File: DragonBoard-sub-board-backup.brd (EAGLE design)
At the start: 85.1 x 54 mm, 77 parts, among them IC1 REG1117, IC2 93AA76A, Q2 8MHz, U1 TXB0108PWR, U2 TXB0108PWR, U3 62674-301121ALF, U4 62674-301121ALF, U5 NC7ST04M5X

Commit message: Done with baord
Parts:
- removed .1UF, .1UF1, .1UF2, .1UF3, .1UF4, 4.7UF, 4.7UF1, 4.7UF2, 4.7UF3, 4.7UF4, 4.7UF5: (no value), rcl:C0402
- added C100, C102, C104, C106, C107, C108, C109, C110: 0.1uF, rcl:C0402
- added C101, C103, C105: 4.7uF, rcl:C0402
- added C31, C32: 0.1uF, rcl:C0805
- added JP11, JP12, JP13: (no value), pinhead:1X04
- C1, C10, C11, C12, C13, C14, C15, C16, C17, C18, C19, C20, C21, C22, C23, C24, C28, C30, C4, C5, C8, C9: value (none) -> 0.1uF
- C2, C3: value (none) -> 0.1Uf
- C25, C26: value (none) -> 30pF
- C27, C29: value (none) -> 4.7uF
- C6, C7: value (none) -> 1uF
- L1, L2: value (none) -> 0.1uH
- Q2: value 8MHz -> 12MHz
- R1: value (none) -> 1K
- R2, R3: value (none) -> 100k
- R4: value (none) -> 12k
- R5: value (none) -> 22k
- U$1: value DRAGON-BOARD -> DRAGON-BOARD-TH; device DragonBoard:DROGENBOARD -> DragonBoard:DROGENBOARD-TH
- moved JP8 91.2 mm to (93.0, 3.43)
- moved C28 79.1 mm to (65.9, 5.59)
- moved C27 64.2 mm to (77.5, 18.7)
- moved L1 60.8 mm to (60.5, 8.51)
- moved R5 60.7 mm to (73.5, 18.2), turned to 270 degrees
- moved U$4 60.1 mm to (75.6, 10.0)
- moved C29 59.4 mm to (82.3, 15.1), turned to 0 degrees
- moved C30 58.8 mm to (66.7, 10.9)
- moved R4 58.8 mm to (66.7, 9.78)
- moved L2 58.8 mm to (60.3, 11.7)
- moved Q2 57.9 mm to (66.9, 16.3), turned to 180 degrees
- moved C25 57.5 mm to (62.9, 19.3)
- moved R1 57.3 mm to (68.3, 3.05)
- moved R2 57.0 mm to (67.1, 3.05)
- moved IC2 56.8 mm to (73.5, 21.8)
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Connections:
- removed net 3.3V: IC2.6
- removed net SBUS_RX: JP8.2, U5.4
- removed net SBUS_TX: JP8.1
- new net ADBUS_RX: JP8.2, U$4.17, U5.4
- new net ADBUS_TX: JP8.1, U$4.16
- new net BDBUS_RX: JP11.2, U$4.27
- new net BDBUS_TX: JP11.1, U$4.26
- new net CDBUS_RX: JP12.2, U$4.39
- new net CDBUS_TX: JP12.1, U$4.38
- new net DDBUS_RX: JP13.2, U$4.52
- new net DDBUS_TX: JP13.1, U$4.48
- net +3.3V: now also C100.1, C101.1, C108.1, C109.1, C110.1, C31.1, C32.1, IC2.6, JP11.3, JP12.3, JP13.3; no longer .1UF.1, .1UF4.1, 4.7UF.1, 4.7UF4.1, 4.7UF5.1
- net GND: now also C100.2, C101.2, C102.2, C103.2, C104.2, C105.2, C106.2, C107.2, C108.2, C109.2, C110.2, C31.2, C32.2, JP11.4, JP12.4, JP13.4; no longer .1UF.2, .1UF1.2, .1UF2.2, .1UF3.2, .1UF4.2, 4.7UF.2, 4.7UF1.2, 4.7UF2.2, 4.7UF3.2, 4.7UF4.2, 4.7UF5.2
- net VCORE: now also C106.1, C107.1; no longer .1UF3.1, 4.7UF3.1
- net VPHY: now also C104.1, C105.1; no longer .1UF2.1, 4.7UF2.1
- net VPLL: now also C102.1, C103.1; no longer .1UF1.1, 4.7UF1.1
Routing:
- net +3.3V: track 264.2 -> 378.5 mm, vias 9 -> 13
- net +5V: track 126.3 -> 171.6 mm, vias 10 -> 12
- net VCORE: track 0.00 -> 41.1 mm
- net GND: track 30.9 -> 65.2 mm, vias 21 -> 51
- net USB_D+: track 17.9 -> 42.8 mm, vias 0 -> 1
- net ADBUS_RX: track 0.00 -> 23.9 mm, vias 0 -> 1
- net DDBUS_RX: track 0.00 -> 21.8 mm, vias 0 -> 2
- net ADBUS_TX: track 0.00 -> 21.3 mm
- net USB_D-: track 18.3 -> 38.9 mm, vias 0 -> 1
- net BDBUS_RX: track 0.00 -> 20.0 mm, vias 0 -> 2
- net BDBUS_TX: track 0.00 -> 18.0 mm, vias 0 -> 2
- net CDBUS_RX: track 0.00 -> 17.9 mm
- net N$11: track 0.00 -> 15.0 mm
- net CDBUS_TX: track 0.00 -> 12.3 mm
- net DDBUS_TX: track 0.00 -> 11.3 mm, vias 0 -> 2
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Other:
- board size 85.1 x 54 mm -> 100 x 54 mm

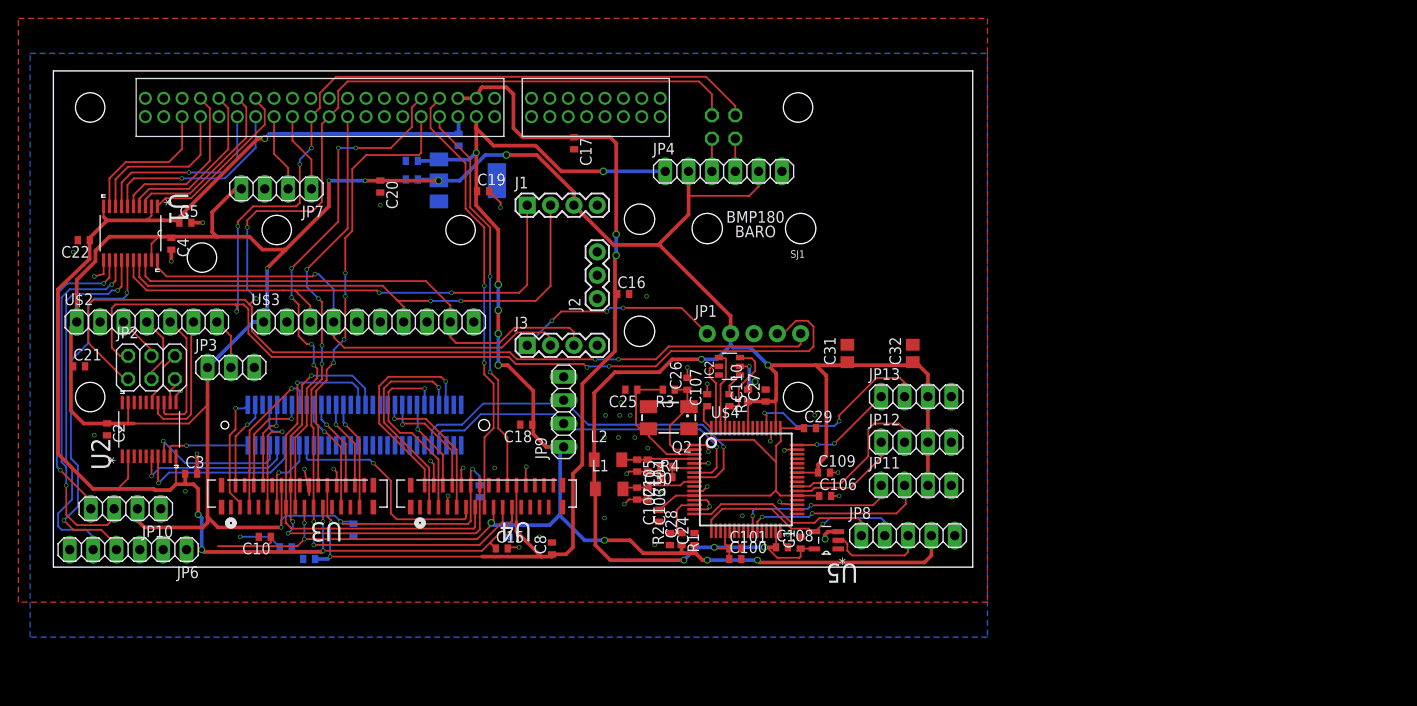
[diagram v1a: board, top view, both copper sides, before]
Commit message: Fixed missing traces and some values. Also added bmp logos.
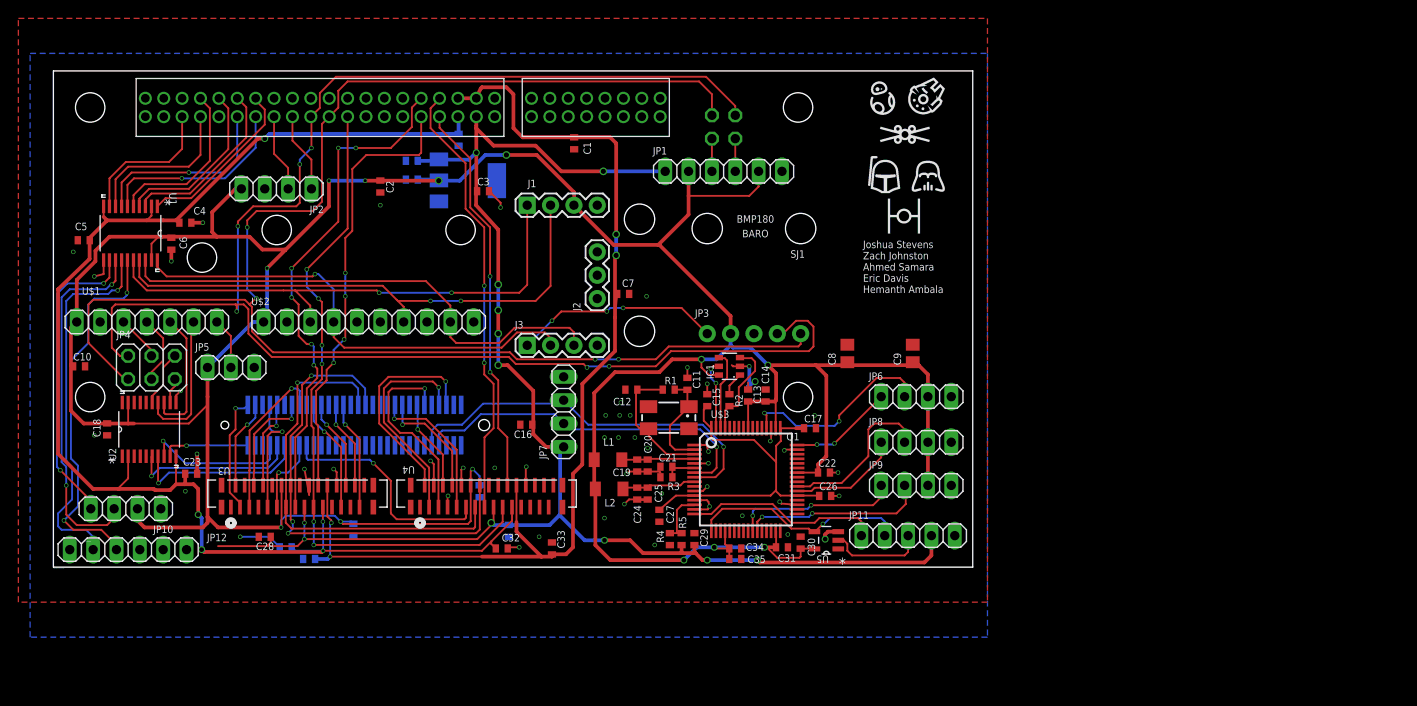
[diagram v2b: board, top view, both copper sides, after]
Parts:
- removed C108, C109, C110: 0.1uF, rcl:C0402
- removed IC2: 93AA76A, microchip:SOT23-6
- removed JP13: (no value), pinhead:1X04
- added C33, C35: 0.1uF, rcl:C0402
- added C34: 4.7uF, rcl:C0402
- added IC100: REG1117, burr-brown:SOT223
- added JP100: (no value), pinhead:2X02
- C101, C103, C27, C29: value 4.7uF -> 0.1uF
- C105: value 4.7uF -> 1uF
- C106: value 0.1uF -> 1uF
- C11, C12: value 0.1uF -> 30pF
- C14, C17, C19: value 0.1uF -> 4.7uF
- C18, C23: value 0.1uF -> 0.1Uf
- C2, C3: value 0.1Uf -> 0.1uF
- C21: value 0.1uF -> NC
- C25: value 30pF -> 4.7uF
- C26: value 30pF -> 0.1uF
- C31, C32: device rcl:C0805 -> rcl:C0402
- C6, C7: value 1uF -> 0.1uF
- C8, C9: device rcl:C0402 -> rcl:C0805
- IC1: value REG1117 -> 93AA76A; device burr-brown:SOT223 -> microchip:SOT23-6
- JP1: device mike-temp:1X05_ROUNDONLY_NOSILK -> pinhead:1X06
- JP11: device pinhead:1X04 -> pinhead:1X05
- JP12: device pinhead:1X04 -> pinhead:1X06
- JP2: device pinhead:2X03 -> pinhead:1X04
- JP3: device pinhead:1X03 -> mike-temp:1X05_ROUNDONLY_NOSILK
- JP4: device pinhead:1X06 -> pinhead:2X03
- JP5: device pinhead:2X02 -> pinhead:1X03
- JP6: device pinhead:1X06 -> pinhead:1X04
- JP8: device pinhead:1X05 -> pinhead:1X04
- R1: value 1K -> NC
- R2: value 100k -> 2k
- R3: value 100k -> 12k
- R4: value 12k -> 10k
- R5: value 22k -> 15K
- U$1: value DRAGON-BOARD-TH -> GY-63; device DragonBoard:DROGENBOARD-TH -> imu:BURO
- U$2: value GY-63 -> GY-9250; device imu:BURO -> imu:IMU
- U$3: value GY-9250 -> FT423H; device imu:IMU -> FT432H:LQFP-64
- U$4: value FT423H -> DRAGON-BOARD-TH; device FT432H:LQFP-64 -> DragonBoard:DROGENBOARD-TH
- moved JP6 87.3 mm to (93.9, 18.5), turned to 0 degrees
- moved JP12 86.5 mm to (8.13, 1.91), turned to 180 degrees
- moved C22 84.4 mm to (83.8, 10.3), turned to 0 degrees
- moved U$4 76.2 mm to (0.00, 0.00), turned to 0 degrees
- moved C9 69.4 mm to (93.5, 23.2), flipped to the top, turned to 90 degrees
- moved JP4 65.8 mm to (10.7, 21.7)
- moved C21 64.8 mm to (66.7, 10.9), turned to 180 degrees
- moved JP5 59.6 mm to (19.3, 21.7), flipped to the top
- moved C106 57.9 mm to (39.0, 44.2), flipped to the bottom
- moved C14 54.7 mm to (77.5, 18.7), flipped to the top, turned to 90 degrees
- moved JP3 51.9 mm to (71.1, 25.4)
- moved C1 49.9 mm to (56.6, 46.1), turned to 270 degrees
- moved C32 49.5 mm to (48.8, 2.03), turned to 0 degrees
- moved C101 48.9 mm to (25.3, 2.16), flipped to the bottom
- moved C23 46.5 mm to (15.0, 10.2), flipped to the top, turned to 0 degrees
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- renumbered Q2 to Q1
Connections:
- net +1.8V: now also C101.1, C107.1, C32.1, C4.1, U$4.LS35; no longer C14.1, C15.1, C22.1, C3.1, U$1.LS35
- net +3.3V: now also C10.1, C103.1, C104.1, C105.1, C14.1, C18.1, C22.1, C30.1, C34.1, C35.1, C6.1, C8.1, C9.1, IC1.6, IC100.2, JP1.5, JP2.4, JP3.2, JP5.1, JP6.3, JP8.3, JP9.3, U$1.1, U$3.20, U$3.31, U$3.42, U$3.50, U$3.56; no longer C1.1, C100.1, C101.1, C108.1, C109.1, C110.1, C12.1, C20.1, C21.1, C27.1, C32.1, C4.1, C7.1, IC1.2, IC2.6, JP11.3, JP12.3, JP13.3, JP3.1, JP4.2, JP4.5, JP7.4, U$3.1, U$4.20, U$4.31, U$4.42, U$4.50, U$4.56
- net +5V: now also C102.1, C106.1, C16.1, C28.1, C29.1, C3.1, IC100.3, JP1.1, JP11.4, JP7.1, R5.2, U$4.LS37; no longer C10.1, C11.1, C18.1, C19.1, C24.1, C6.1, IC1.3, JP4.1, JP8.4, JP9.1, R1.2, U$1.LS37
- net ADBUS_RX: now also JP11.2, U$3.17; no longer JP8.2, U$4.17
- net ADBUS_TX: now also JP11.1, U$3.16; no longer JP8.1, U$4.16
- net BDBUS_RX: now also JP9.2, U$3.27; no longer JP11.2, U$4.27
- net BDBUS_TX: now also JP9.1, U$3.26; no longer JP11.1, U$4.26
- net CAM_SCL: now also U$4.HS32; no longer U$1.HS32
- net CAM_SDA: now also U$4.HS34; no longer U$1.HS34
- net CDBUS_RX: now also JP8.2, U$3.39; no longer JP12.2, U$4.39
- net CDBUS_TX: now also JP8.1, U$3.38; no longer JP12.1, U$4.38
- net CDC_HPH_L: now also U$4.A10; no longer U$1.A10
- net CDC_HPH_R: now also U$4.A8; no longer U$1.A8
- net CDC_HPH_REF: now also U$4.A9; no longer U$1.A9
- net CDC_HS_DET: now also U$4.A11; no longer U$1.A11
- net CDC_MIC2_P: now also U$4.A6; no longer U$1.A6
- net CDC_MIC3_P: now also U$4.A7; no longer U$1.A7
- net CDC_MIC_BIAS1: now also U$4.A12; no longer U$1.A12
- net CON_RX: now also JP12.4; no longer JP6.4
- net CON_TX: now also JP12.5; no longer JP6.5
- net CSI0_C+: now also U$4.HS2; no longer U$1.HS2
- net CSI0_C-: now also U$4.HS4; no longer U$1.HS4
- net CSI0_D0+: now also U$4.HS8; no longer U$1.HS8
- net CSI0_D0-: now also U$4.HS10; no longer U$1.HS10
- net CSI0_D1+: now also U$4.HS14; no longer U$1.HS14
- net CSI0_D1-: now also U$4.HS16; no longer U$1.HS16
- net CSI0_D2+: now also U$4.HS20; no longer U$1.HS20
- net CSI0_D2-: now also U$4.HS22; no longer U$1.HS22
- net CSI0_D3+: now also U$4.HS26; no longer U$1.HS26
- net CSI0_D3-: now also U$4.HS28; no longer U$1.HS28
- net CSI1_C+: now also U$4.HS54; no longer U$1.HS54
- net CSI1_C-: now also U$4.HS56; no longer U$1.HS56
- net CSI1_D0+: now also U$4.HS42; no longer U$1.HS42
- net CSI1_D0-: now also U$4.HS44; no longer U$1.HS44
- net CSI1_D1+: now also U$4.HS48; no longer U$1.HS48
- net CSI1_D1-: now also U$4.HS50; no longer U$1.HS50
- net DDBUS_RX: now also JP6.2, U$3.52; no longer JP13.2, U$4.52
- net DDBUS_TX: now also JP6.1, U$3.48; no longer JP13.1, U$4.48
- net DSI_BLCTRL: now also U$4.LS28; no longer U$1.LS28
- net DSI_CLK+: now also U$4.HS21; no longer U$1.HS21
- net DSI_CLK-: now also U$4.HS23; no longer U$1.HS23
- net DSI_D0+: now also U$4.HS27; no longer U$1.HS27
- net DSI_D0-: now also U$4.HS29; no longer U$1.HS29
- net DSI_D1+: now also U$4.HS33; no longer U$1.HS33
- net DSI_D1-: now also U$4.HS35; no longer U$1.HS35
- net DSI_D2+: now also U$4.HS39; no longer U$1.HS39
- net DSI_D2-: now also U$4.HS41; no longer U$1.HS41
- net DSI_D3+: now also U$4.HS45; no longer U$1.HS45
- net DSI_D3-: now also U$4.HS47; no longer U$1.HS47
- net EECLK: now also IC1.4, U$3.62; no longer IC2.4, U$4.62
- net EECS: now also IC1.5, U$3.63; no longer IC2.5, U$4.63
- net EEDATA: now also IC1.3, R2.2, U$3.61; no longer IC2.3, R5.2, U$4.61
- net FLASH: now also U$4.LS23; no longer U$1.LS23
- net GND: now also C33.2, C34.2, C35.2, IC1.2, IC100.1, JP1.6, JP11.5, JP12.1, JP2.3, JP5.3, JP6.4, JP7.4, JP8.4, R3.1, U$1.2, U$2.10, U$3.1, U$3.11, U$3.13, U$3.15, U$3.25, U$3.35, U$3.47, U$3.5, U$3.51, U$4.A4, U$4.HS12, U$4.HS13, U$4.HS18, U$4.HS19, U$4.HS24, U$4.HS25, U$4.HS30, U$4.HS31, U$4.HS37, U$4.HS43, U$4.HS46, U$4.HS49, U$4.HS52, U$4.HS55, U$4.HS58, U$4.HS6, U$4.LS1, U$4.LS2, U$4.LS39, U$4.LS40; no longer C108.2, C109.2, C110.2, IC1.1, IC2.2, JP1.3, JP11.4, JP12.4, JP13.4, JP4.6, JP6.1, JP7.3, JP8.5, R2.1, U$1.A4, U$1.HS12, U$1.HS13, U$1.HS18, U$1.HS19, U$1.HS24, U$1.HS25, U$1.HS30, U$1.HS31, U$1.HS37, U$1.HS43, U$1.HS46, U$1.HS49, U$1.HS52, U$1.HS55, U$1.HS58, U$1.HS6, U$1.LS1, U$1.LS2, U$1.LS39, U$1.LS40, U$3.2, U$4.1, U$4.10, U$4.11, U$4.13, U$4.15, U$4.25, U$4.35, U$4.47, U$4.5, U$4.51
- net GND_CFILT: now also U$4.A5; no longer U$1.A5
- net GPIO_110: now also U$4.LS16; no longer U$1.LS16
- net GPIO_113: now also U$4.LS18; no longer U$1.LS18
- net GPIO_114: now also U$4.LS20; no longer U$1.LS20
- net GPIO_115: now also U$4.LS27; no longer U$1.LS27
- net GPIO_12: now also U$4.LS24; no longer U$1.LS24
- net GPIO_13: now also U$4.LS25; no longer U$1.LS25
- net GPIO_24: now also U$4.LS29; no longer U$1.LS29
- net GPIO_25: now also U$4.LS30; no longer U$1.LS30
- net GPIO_69: now also U$4.LS26; no longer U$1.LS26
- net HSIC_DATA: now also U$4.HS59; no longer U$1.HS59
- net HSIC_STR: now also U$4.HS57; no longer U$1.HS57
- net I2C0_SCL: now also JP2.2, U$4.LS15; no longer JP7.2, U$1.LS15
- net I2C0_SDA: now also JP2.1, U$4.LS17; no longer JP7.1, U$1.LS17
- net I2C1_SCL: now also JP100.2, JP3.4, JP4.2, U$4.LS19; no longer JP1.4, JP2.2, JP5.2, U$1.LS19
- net I2C1_SDA: now also JP100.4, JP3.5, JP4.1, U$4.LS21; no longer JP1.5, JP2.1, JP5.4, U$1.LS21
- net I2C3_SCL: now also U$4.HS36; no longer U$1.HS36
- net I2C3_SDA: now also U$4.HS38; no longer U$1.HS38
- net MCLK0: now also U$4.HS15; no longer U$1.HS15
- net MCLK1: now also U$4.HS17; no longer U$1.HS17
- net N$1: now also JP5.2, U$1.7; no longer JP3.2, U$2.7
- net N$10: now also U$2.6; no longer U$3.6
- net N$11: now also C12.1, R1.2, U$3.3; no longer C25.1, R3.2, U$4.3
- net N$12: now also U$2.8; no longer U$3.8
- net N$14: now also IC1.1, R2.1; no longer IC2.1, R5.1
- net N$17: now also R4.2, R5.1, U$3.14; no longer R1.1, R2.2, U$4.14
- net N$2: now also JP4.3, U$1.4; no longer JP2.3, U$2.4
- net N$3: now also JP4.4, U$1.3; no longer JP2.4, U$2.3
- net N$4: now also JP1.4, JP100.1; no longer JP4.4, JP5.1
- net N$5: now also JP1.3, JP100.3; no longer JP4.3, JP5.3
- net N$6: now also C21.1, R3.2, U$3.6; no longer C30.1, R4.2, U$4.6
- net N$7: now also C11.1, R1.1, U$3.2; no longer C26.1, R3.1, U$4.2
- net N$8: now also U$2.5; no longer U$3.5
- net N$9: now also U$4.A15; no longer U$1.A15
- net ON: now also U$4.LS4; no longer U$1.LS4
- net RESET0: now also U$4.LS31; no longer U$1.LS31
- net RESET1: now also U$4.LS33; no longer U$1.LS33
- net RESIN: now also U$4.LS6; no longer U$1.LS6
- net SBUS: now also JP11.3; no longer JP8.3
- net SPI0_CLK: now also U$4.LS8; no longer U$1.LS8
- net SPI0_CS_N: now also U$4.LS12; no longer U$1.LS12
- net SPI0_MISO: now also U$4.LS10; no longer U$1.LS10
- net SPI0_MOSI: now also U$4.LS14; no longer U$1.LS14
- net SPI1_CLK: now also U$4.HS9; no longer U$1.HS9
- net SPI1_CS: now also U$4.HS7; no longer U$1.HS7
- net SPI1_MISO: now also U$4.HS11; no longer U$1.HS11
- net SPI1_MOSI: now also U$4.HS1; no longer U$1.HS1
- net SPI_A_CLK: now also U$2.3; no longer U$3.3
- net SPI_A_CS: now also U$2.9; no longer U$3.9
- net SPI_A_MISO: now also U$2.7; no longer U$3.7
- net SPI_A_MOSI: now also U$2.4; no longer U$3.4
- net SPI_B_CLK: now also JP4.6; no longer JP2.6
- net SPI_B_CS: now also U$1.5; no longer U$2.5
- net SPI_B_MISO: now also U$1.6; no longer U$2.6
- net SPI_B_MOSI: now also JP4.5; no longer JP2.5
- net SPKR_OUT_M: now also U$4.A2; no longer U$1.A2
- net SPKR_OUT_P: now also U$4.A1; no longer U$1.A1
- net STANDBY0: now also U$4.LS32; no longer U$1.LS32
- net STANDBY1: now also U$4.LS34; no longer U$1.LS34
- net SYS_DCIN: now also C1.1, C100.1, C33.1, C7.1, U$4.LS36, U$4.LS38; no longer C16.1, C17.1, C8.1, C9.1, U$1.LS36, U$1.LS38
- net UART0_CTS: now also U$4.LS3; no longer U$1.LS3
- net UART0_RX: now also U$4.LS7; no longer U$1.LS7
- net UART0_TX: now also U$4.LS5; no longer U$1.LS5
- net UART1_RX: now also U$4.LS13; no longer U$1.LS13
- net UART1_TX: now also U$4.LS11; no longer U$1.LS11
- net UART_RTS: now also U$4.LS9; no longer U$1.LS9
- net USB_D+: now also JP7.3, U$3.8, U$4.HS51; no longer JP9.3, U$1.HS51, U$4.8
- net USB_D-: now also JP7.2, U$3.7, U$4.HS53; no longer JP9.2, U$1.HS53, U$4.7
- net VCORE: now also C15.1, C17.1, C26.1, C27.1, U$3.12, U$3.37, U$3.49, U$3.64; no longer C106.1, C107.1, C28.1, C29.1, U$4.12, U$4.37, U$4.49, U$4.64
- net VDDIO: now also JP3.1; no longer JP1.1
- net VPHY: now also C19.1, C20.1, L1.2, U$3.4; no longer C104.1, C105.1, L2.2, U$4.4
- net VPH_PWR: now also U$4.A3; no longer U$1.A3
- net VPLL: now also C24.1, C25.1, L2.2, U$3.9; no longer C102.1, C103.1, L1.2, U$4.9
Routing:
- net +3.3V: track 378.5 -> 381.7 mm
- net EECS: track 7.88 -> 7.70 mm, vias 0 -> 2
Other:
- board text added: "/home/ztjohnst/Pictures/iconsv1.bmp"
- board text added: "Joshua Stevens Zach Johnston Ahmed Samara Eric Davis Hemanth Ambala"

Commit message: Fixed more of Josh's fuck ups.
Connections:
- removed net GND_CFILT: U$4.A5
- net GND: now also U$4.A5
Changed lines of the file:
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@@
 <contactref element="C21" pad="2"/>
 <contactref element="R3" pad="1"/>
+<contactref element="U$4" pad="A5"/>
+<wire x1="54" y1="51" x2="56" y2="49" width="0" layer="19" extent="1-1"/>
 </signal>
 <signal name="UART0_TX">
@@
 <contactref element="U$4" pad="A3"/>
 </signal>
-<signal name="GND_CFILT">
-<contactref element="U$4" pad="A5"/>
-</signal>
 <signal name="CDC_MIC3_P">
